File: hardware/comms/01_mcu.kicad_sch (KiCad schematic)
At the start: 37 parts, among them J2 LEFT, J3 RIGHT, J4 SWD, SW1 BOOTSEL, SW2 RUN, U1 RP2350A, U3 W25Q16JVUXIQ, Y1 12MHz

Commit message: Rev A close-out: LCSC numbers, assembly sidecar, regen script
hardware/parts/lcsc.csv gives every placed part an LCSC number, looked
up in JLCPCB's library on 2026-10-02, and pcbview shows them in the
part pane. tools/assembly.py exports IPC-2581, writes the boardvis
sidecar (pin-1 evidence per polarised part) and runs boardvis: 0 errors.
tools/regen.py runs DRC, ERC, the netlist comparison and boardvis, then
rebuilds the viewer and the page's status line. Mounting holes are out
of the BOM on the sheets, as their footprints say. Viewer rebuilt.

Co-Authored-By: Claude Fable 5.1 <noreply@anthropic.com>
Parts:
- H1, H2, H3, H4: now left out of the parts list
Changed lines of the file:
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@@
 		(unit 1)
 		(exclude_from_sim no)
-		(in_bom yes)
+		(in_bom no)
 		(on_board yes)
 		(dnp no)
@@
 		(unit 1)
 		(exclude_from_sim no)
-		(in_bom yes)
+		(in_bom no)
 		(on_board yes)
 		(dnp no)
@@
 		(unit 1)
 		(exclude_from_sim no)
-		(in_bom yes)
+		(in_bom no)
 		(on_board yes)
 		(dnp no)
@@
 		(unit 1)
 		(exclude_from_sim no)
-		(in_bom yes)
+		(in_bom no)
 		(on_board yes)
 		(dnp no)

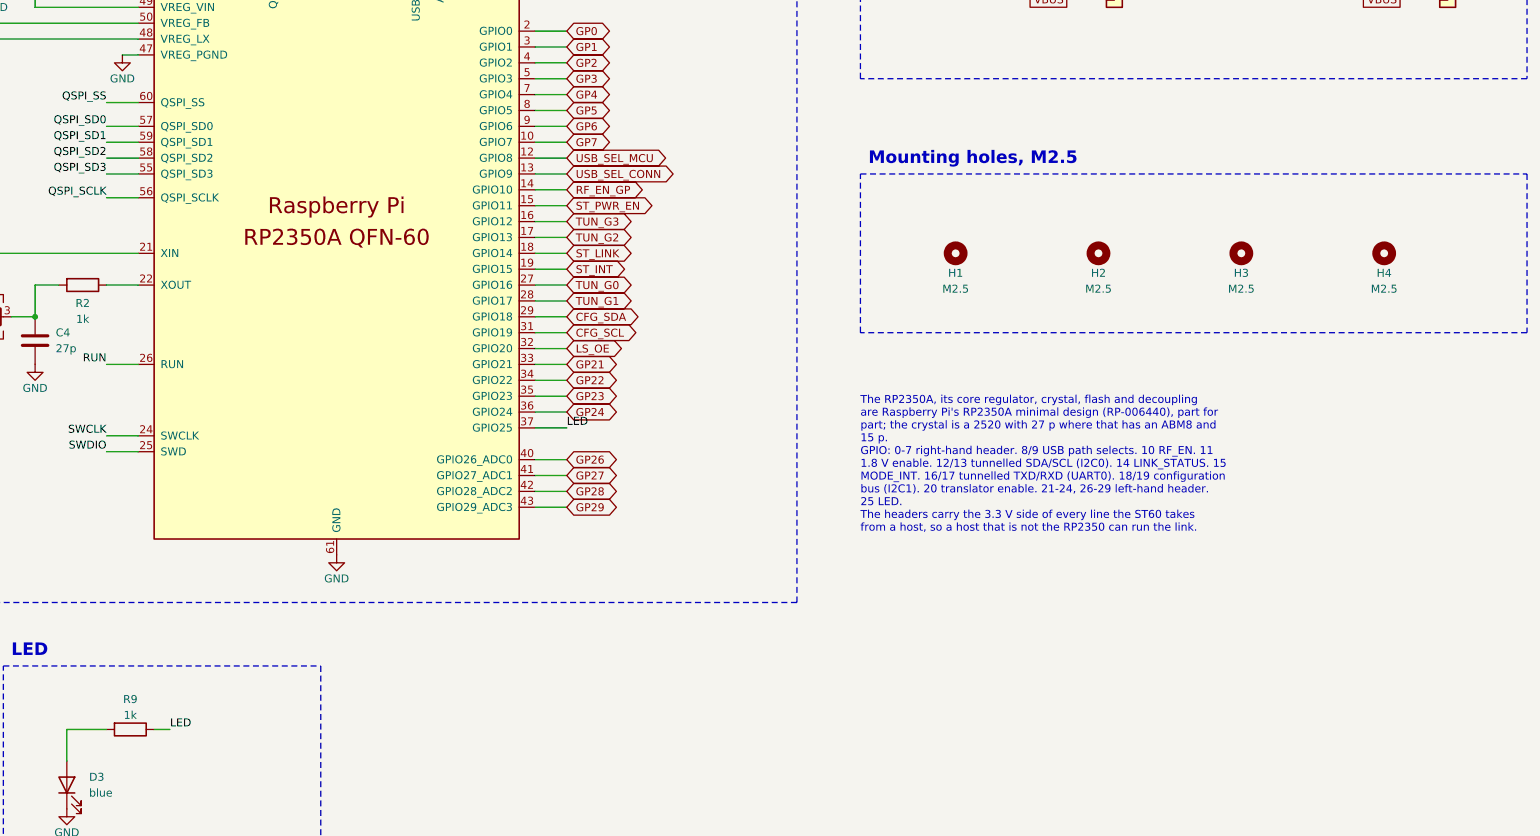
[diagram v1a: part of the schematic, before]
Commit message: Rev A after review: ST's antenna ground, 1.8 V rail, pull-ups, 90 ohm pairs
Two independent reviews (schematic against the data sheets, layout
against JLCPCB's limits and ST's B2379A) found no blocker and a dozen
things worth fixing. The board is regenerated and routed again.

Layout: the ST60's ball field is laid as ST lays it -- nine signals
straight out through one side of the ring, the supply along the top --
and the island and fence vias are ST's own, from its drill file (33 and
45 fit, where rev A had 13 and 15). USB pairs on the back 0.28/0.16 mm;
the +1V8 plane redrawn so the pair to the repeater has +3V3 under it
throughout. ST60 mask openings 0.30 mm. Silkscreen to JLCPCB's sizes.
VBUS joined on the back, not under the USB-C shell. Three fiducials.

Schematic: 1.8 uF on +1V8 and its enable pulled down; 4k7 on MODE_INT;
4k7 pull-ups on the 1.8 V side of the four I2C lines; 220 R on the LEDs.

README has the review table, what was left as it is, and ordering notes
(Standard PCBA, 0.10 mm stencil, nylon standoffs, firmware sequencing).

Co-Authored-By: Claude Fable 5.1 <noreply@anthropic.com>
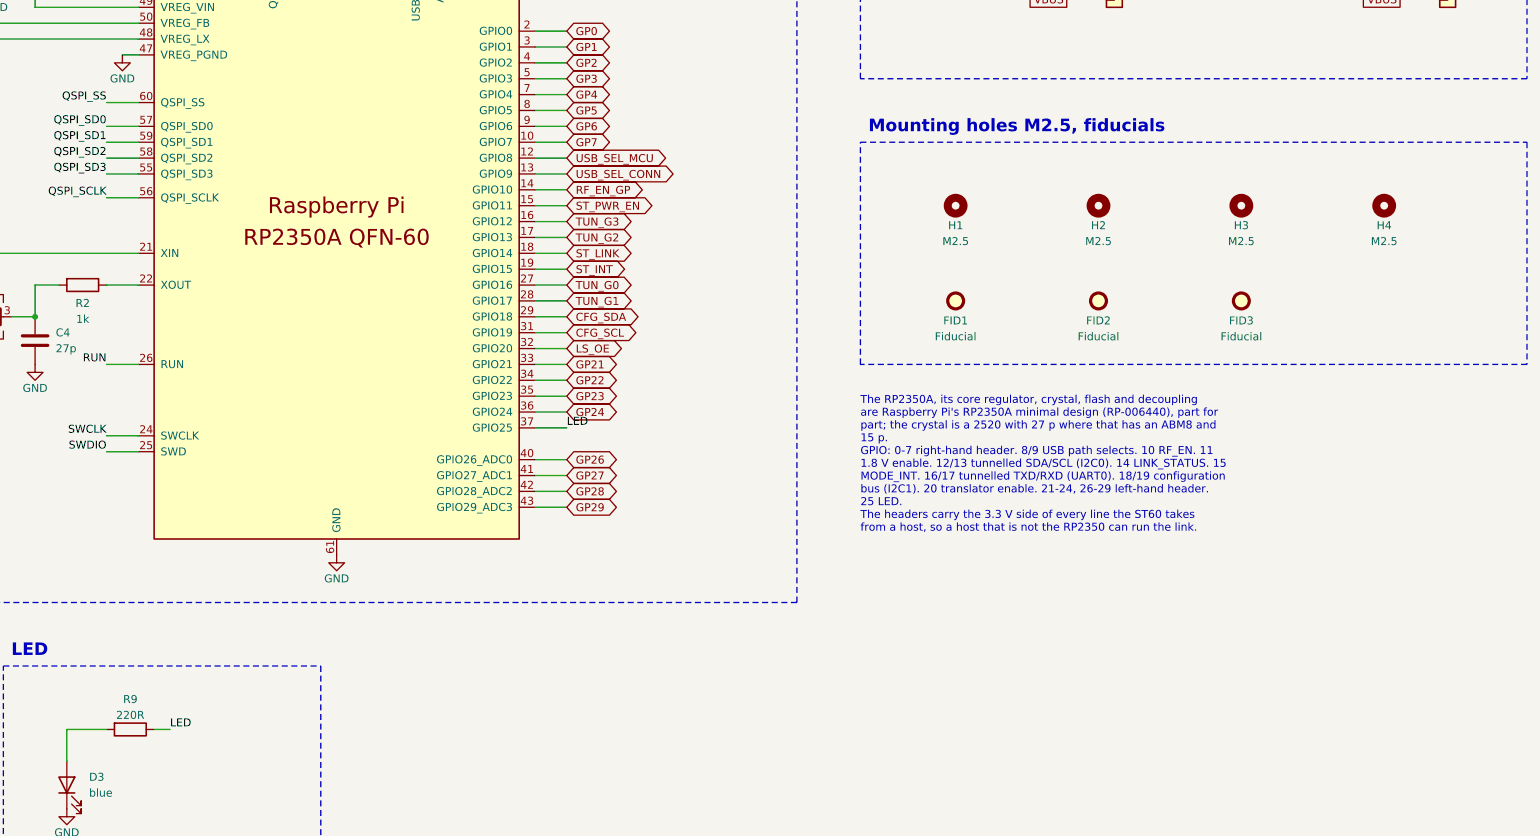
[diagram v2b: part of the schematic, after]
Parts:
- added FID1, FID2, FID3: Fiducial, Fiducial:Fiducial_1mm_Mask2mm, symbol Mechanical:Fiducial
- R9: value 1k -> 220R
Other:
- note added: "Mounting holes M2.5, fiducials"
- note removed: "Mounting holes, M2.5"
- moved on the sheet: H1, H2, H3, H4
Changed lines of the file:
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@@
 			(at 170.1800 202.1840 90)
 			(effects (font (size 1.27 1.27))))
-		(property "Value" "1k"
+		(property "Value" "220R"
 			(at 170.1800 204.7240 90)
 			(effects (font (size 1.27 1.27))))
@@
 	(symbol
 		(lib_id "Mechanical:MountingHole")
-		(at 302.2600 130.8100 0)
+		(at 302.2600 123.1900 0)
 		(unit 1)
 		(exclude_from_sim no)
@@
 		(dnp no)
 		(property "Reference" "H1"
-			(at 302.2600 133.9800 0)
+			(at 302.2600 126.3600 0)
 			(effects (font (size 1.27 1.27))))
 		(property "Value" "M2.5"
-			(at 302.2600 136.5200 0)
-			(effects (font (size 1.27 1.27))))
-		(property "Footprint" "MountingHole:MountingHole_2.7mm_M2.5" (at 302.2600 130.8100 0)
-			(effects (font (size 1.27 1.27)) (hide yes)))
-		(property "Datasheet" "~" (at 302.2600 130.8100 0)
+			(at 302.2600 128.9000 0)
+			(effects (font (size 1.27 1.27))))
+		(property "Footprint" "MountingHole:MountingHole_2.7mm_M2.5" (at 302.2600 123.1900 0)
+			(effects (font (size 1.27 1.27)) (hide yes)))
+		(property "Datasheet" "~" (at 302.2600 123.1900 0)
 			(effects (font (size 1.27 1.27)) (hide yes)))
 		(instances
@@
 	(symbol
 		(lib_id "Mechanical:MountingHole")
-		(at 325.1200 130.8100 0)
+		(at 325.1200 123.1900 0)
 		(unit 1)
 		(exclude_from_sim no)
@@
 		(dnp no)
 		(property "Reference" "H2"
-			(at 325.1200 133.9800 0)
+			(at 325.1200 126.3600 0)
 			(effects (font (size 1.27 1.27))))
 		(property "Value" "M2.5"
-			(at 325.1200 136.5200 0)
-			(effects (font (size 1.27 1.27))))
-		(property "Footprint" "MountingHole:MountingHole_2.7mm_M2.5" (at 325.1200 130.8100 0)
-			(effects (font (size 1.27 1.27)) (hide yes)))
-		(property "Datasheet" "~" (at 325.1200 130.8100 0)
+			(at 325.1200 128.9000 0)
+			(effects (font (size 1.27 1.27))))
+		(property "Footprint" "MountingHole:MountingHole_2.7mm_M2.5" (at 325.1200 123.1900 0)
+			(effects (font (size 1.27 1.27)) (hide yes)))
+		(property "Datasheet" "~" (at 325.1200 123.1900 0)
 			(effects (font (size 1.27 1.27)) (hide yes)))
 		(instances
@@
 	(symbol
 		(lib_id "Mechanical:MountingHole")
-		(at 347.9800 130.8100 0)
+		(at 347.9800 123.1900 0)
 		(unit 1)
 		(exclude_from_sim no)
@@
 		(dnp no)
 		(property "Reference" "H3"
-			(at 347.9800 133.9800 0)
+			(at 347.9800 126.3600 0)
 			(effects (font (size 1.27 1.27))))
 		(property "Value" "M2.5"
-			(at 347.9800 136.5200 0)
-			(effects (font (size 1.27 1.27))))
-		(property "Footprint" "MountingHole:MountingHole_2.7mm_M2.5" (at 347.9800 130.8100 0)
-			(effects (font (size 1.27 1.27)) (hide yes)))
-		(property "Datasheet" "~" (at 347.9800 130.8100 0)
+			(at 347.9800 128.9000 0)
+			(effects (font (size 1.27 1.27))))
+		(property "Footprint" "MountingHole:MountingHole_2.7mm_M2.5" (at 347.9800 123.1900 0)
+			(effects (font (size 1.27 1.27)) (hide yes)))
+		(property "Datasheet" "~" (at 347.9800 123.1900 0)
 			(effects (font (size 1.27 1.27)) (hide yes)))
 		(instances
@@
 	(symbol
 		(lib_id "Mechanical:MountingHole")
-		(at 370.8400 130.8100 0)
+		(at 370.8400 123.1900 0)
 		(unit 1)
 		(exclude_from_sim no)
@@
 		(dnp no)
 		(property "Reference" "H4"
-			(at 370.8400 133.9800 0)
+			(at 370.8400 126.3600 0)
 			(effects (font (size 1.27 1.27))))
 		(property "Value" "M2.5"
-			(at 370.8400 136.5200 0)
-			(effects (font (size 1.27 1.27))))
-		(property "Footprint" "MountingHole:MountingHole_2.7mm_M2.5" (at 370.8400 130.8100 0)
-			(effects (font (size 1.27 1.27)) (hide yes)))
-		(property "Datasheet" "~" (at 370.8400 130.8100 0)
+			(at 370.8400 128.9000 0)
+			(effects (font (size 1.27 1.27))))
+		(property "Footprint" "MountingHole:MountingHole_2.7mm_M2.5" (at 370.8400 123.1900 0)
+			(effects (font (size 1.27 1.27)) (hide yes)))
+		(property "Datasheet" "~" (at 370.8400 123.1900 0)
 			(effects (font (size 1.27 1.27)) (hide yes)))
 		(instances
@@
 				(path "/8132f9b4-61be-5b7f-9744-e0828e24db53/1ba61b7e-b878-52da-84e3-0f73bc410a8e"
 					(reference "H4") (unit 1)
+				)
+			)
+		)
+	)
+	(symbol
+		(lib_id "Mechanical:Fiducial")
+		(at 302.2600 138.4300 0)
+		(unit 1)
+		(exclude_from_sim no)
+		(in_bom no)
+		(on_board yes)
+		(dnp no)
+		(property "Reference" "FID1"
+			(at 302.2600 141.6000 0)
+			(effects (font (size 1.27 1.27))))
+		(property "Value" "Fiducial"
+			(at 302.2600 144.1400 0)
+			(effects (font (size 1.27 1.27))))
+		(property "Footprint" "Fiducial:Fiducial_1mm_Mask2mm" (at 302.2600 138.4300 0)
+			(effects (font (size 1.27 1.27)) (hide yes)))
+		(property "Datasheet" "~" (at 302.2600 138.4300 0)
+			(effects (font (size 1.27 1.27)) (hide yes)))
+		(instances
+			(project "comms"
+				(path "/8132f9b4-61be-5b7f-9744-e0828e24db53/1ba61b7e-b878-52da-84e3-0f73bc410a8e"
+					(reference "FID1") (unit 1)
+				)
+			)
+		)
+	)
+	(symbol
+		(lib_id "Mechanical:Fiducial")
+		(at 325.1200 138.4300 0)
+		(unit 1)
+		(exclude_from_sim no)
+		(in_bom no)
+		(on_board yes)
+		(dnp no)
+		(property "Reference" "FID2"
+			(at 325.1200 141.6000 0)
+			(effects (font (size 1.27 1.27))))
+		(property "Value" "Fiducial"
+			(at 325.1200 144.1400 0)
+			(effects (font (size 1.27 1.27))))
+		(property "Footprint" "Fiducial:Fiducial_1mm_Mask2mm" (at 325.1200 138.4300 0)
+			(effects (font (size 1.27 1.27)) (hide yes)))
+		(property "Datasheet" "~" (at 325.1200 138.4300 0)
+			(effects (font (size 1.27 1.27)) (hide yes)))
+		(instances
+			(project "comms"
+				(path "/8132f9b4-61be-5b7f-9744-e0828e24db53/1ba61b7e-b878-52da-84e3-0f73bc410a8e"
+					(reference "FID2") (unit 1)
+				)
+			)
+		)
+	)
+	(symbol
+		(lib_id "Mechanical:Fiducial")
+		(at 347.9800 138.4300 0)
+		(unit 1)
+		(exclude_from_sim no)
+		(in_bom no)
+		(on_board yes)
+		(dnp no)
+		(property "Reference" "FID3"
+			(at 347.9800 141.6000 0)
+			(effects (font (size 1.27 1.27))))
+		(property "Value" "Fiducial"
+			(at 347.9800 144.1400 0)
+			(effects (font (size 1.27 1.27))))
+		(property "Footprint" "Fiducial:Fiducial_1mm_Mask2mm" (at 347.9800 138.4300 0)
+			(effects (font (size 1.27 1.27)) (hide yes)))
+		(property "Datasheet" "~" (at 347.9800 138.4300 0)
+			(effects (font (size 1.27 1.27)) (hide yes)))
+		(instances
+			(project "comms"
+				(path "/8132f9b4-61be-5b7f-9744-e0828e24db53/1ba61b7e-b878-52da-84e3-0f73bc410a8e"
+					(reference "FID3") (unit 1)
 				)
 			)
@@
 		(effects (font (size 2.0 2.0) (bold yes)) (justify left bottom))
 )
-	(rectangle (start 287.0200 118.1100) (end 393.7000 143.5100)
+	(rectangle (start 287.0200 113.0300) (end 393.7000 148.5900)
 		(stroke (width 0.1524) (type dash) (color 72 72 72 1))
 		(fill (type none)))
-	(text "Mounting holes, M2.5" (exclude_from_sim no)
-		(at 288.2900 116.8400 0)
+	(text "Mounting holes M2.5, fiducials" (exclude_from_sim no)
+		(at 288.2900 111.7600 0)
 		(effects (font (size 2.0 2.0) (bold yes)) (justify left bottom))
 )
